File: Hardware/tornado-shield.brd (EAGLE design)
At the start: 439.4 x 100 mm, 30 parts, among them CON1 ROV_SHIELD_V2, Q1 DMP2012SN-7, U1 LM2678S-5.0, U2 LM3409HV'LM3409HV'

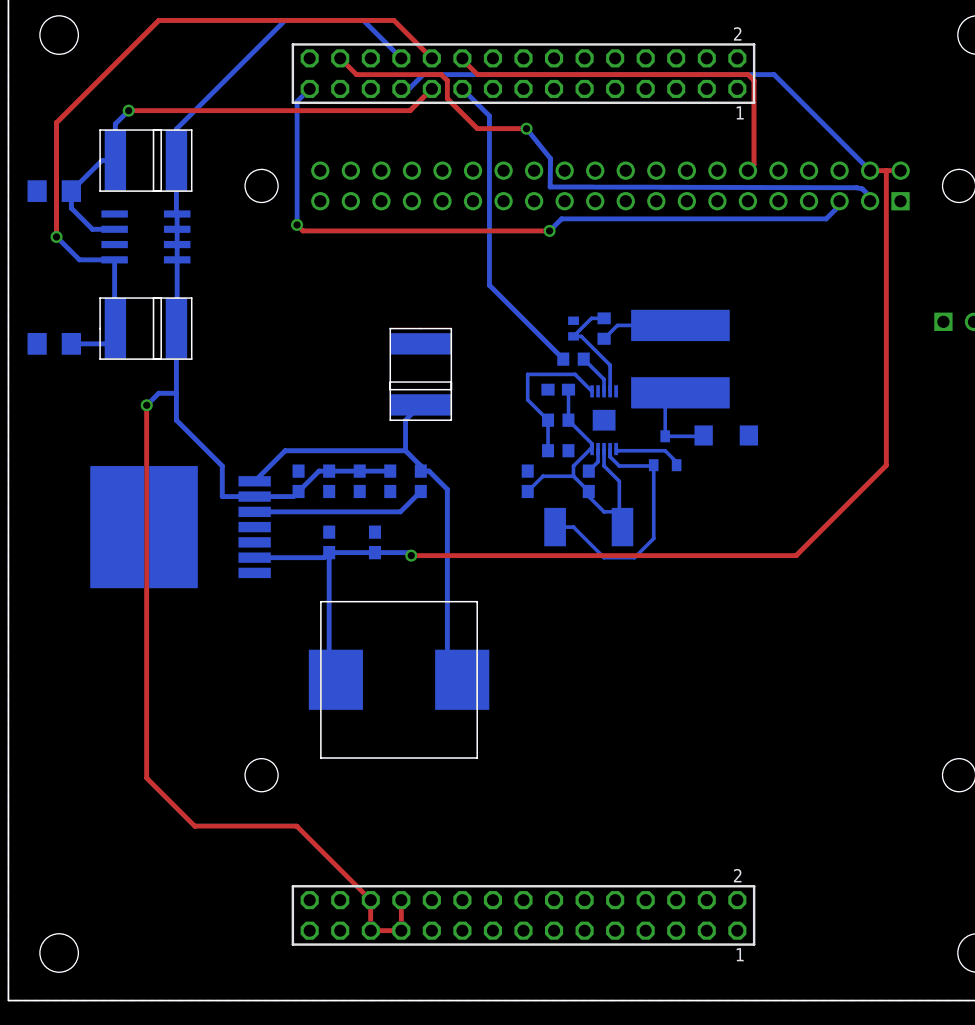
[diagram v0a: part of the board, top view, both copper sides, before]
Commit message: Continued to finish Shield
Still needs Pi Pinout
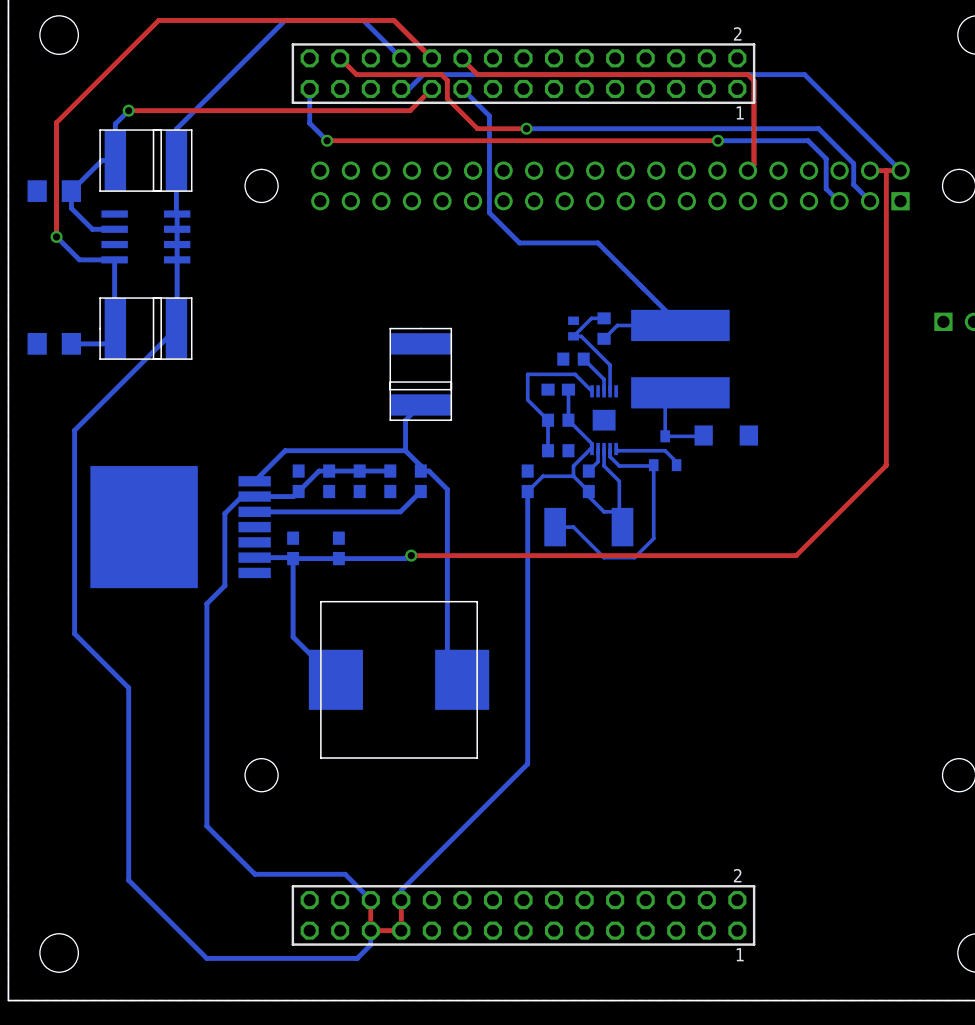
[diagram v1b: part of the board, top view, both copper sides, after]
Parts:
- moved C2 3.04 mm to (23.7, 37.6)
- moved C3 3.04 mm to (27.5, 37.6)
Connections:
- removed net V_IN: C_F.1, C_IN1.1, C_IN2.1, R_SNS.2, R_UV2.2, U2.10, U2.8
- removed net V_OUT: L2.2, R_OFF.1
- new net LED_CON: R_PD.1
- net +12V: now also C_F.1, C_IN1.1, C_IN2.1, R_SNS.2, R_UV2.2, U2.10, U2.8
- net LED_PWM: now also L2.2, R_OFF.1; no longer R_PD.1
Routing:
- net +12V: track 135.1 -> 245.6 mm, vias 1 -> 0
- net V_IN: track 25.5 -> 0.00 mm
- net LED_PWM: track 25.9 -> 37.8 mm
- net NAV_SCL: track 58.3 -> 51.1 mm
- net V_OUT: track 6.81 -> 0.00 mm
- net +5V: track 136.6 -> 141.6 mm
- net NAV_SDA: track 51.6 -> 50.9 mm

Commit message: Wrapping up initial board layout
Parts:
- added RPD, RPD1: 1k, DiscreteComponents:R0603
- moved L1 1.50 mm to (31.0, 26.7)
- moved U$4 0.50 mm to (11.4, 55.4)
- moved U$5 0.50 mm to (11.4, 70.3)
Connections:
- removed net LED_PMW: CON1.18
- removed net N$23: CON1.14
- removed net SCL: CON1.20
- removed net SDA: CON1.22
- new net +3V3: U$2.1
- new net SONAR_TIMER: CON1.14, U$2.36
- net GND: now also RPD.1, RPD1.1
- net GPIO: now also U$2.7
- net GPIO2: now also U$2.11
- net GPIO3: now also U$2.13
- net GPIO4: now also U$2.15
- net GPIO5: now also U$2.31
- net GPIO6: now also U$2.38
- net GPIO7: now also U$2.40
- net LED_CON: now also U$2.33
- net NAV_SCL: now also CON1.20
- net NAV_SDA: now also CON1.22
- net SOL1_IN: now also RPD1.2, U$2.35
- net SOL2_IN: now also RPD.2, U$2.37
- net SONAR_PWM: now also U$2.32
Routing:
- net GPIO: track 0.00 -> 97.5 mm
- net GPIO2: track 0.00 -> 94.8 mm
- net NAV_SDA: track 50.9 -> 145.4 mm, vias 1 -> 2
- net GPIO3: track 0.00 -> 90.2 mm
- net GPIO4: track 0.00 -> 80.7 mm
- net GPIO7: track 0.00 -> 67.3 mm, vias 0 -> 2
- net SONAR_TIMER: track 0.00 -> 66.6 mm, vias 0 -> 2
- net NAV_SCL: track 51.1 -> 117.3 mm
- net GPIO5: track 0.00 -> 63.5 mm, vias 0 -> 3
- net GPIO6: track 0.00 -> 56.3 mm, vias 0 -> 1
- net SOL1_IN: track 0.00 -> 34.0 mm, vias 0 -> 2
- net SOL2_IN: track 0.00 -> 27.0 mm, vias 0 -> 2
- net SONAR_PWM: track 0.00 -> 21.1 mm
- net LED_CON: track 0.00 -> 18.3 mm
- net +12V: track 245.6 -> 249.2 mm, vias 0 -> 1
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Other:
- board size 439.4 x 100 mm -> 84.9 x 84 mm

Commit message: Board Design Rev 1.0
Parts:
- moved R_UV1 0.50 mm to (45.7, 46.2)
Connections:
- removed net KJ: CON1.77
- removed net N$10: CON1.1
- removed net N$11: CON1.78
- removed net N$24: CON1.13
- removed net N$25: CON1.12
- removed net N$26: CON1.11
- removed net N$27: CON1.10
- removed net N$28: CON1.9
- removed net N$29: CON1.8
- removed net N$30: CON1.7
- removed net N$31: CON1.6
- removed net N$32: CON1.5
- removed net N$33: CON1.4
- removed net N$34: CON1.3
- removed net N$37: CON1.76
- removed net N$38: CON1.75
- removed net N$39: CON1.74
- removed net N$40: CON1.73
- removed net N$41: CON1.72
- removed net N$42: CON1.71
- removed net N$43: CON1.70
- removed net N$44: CON1.69
- removed net N$45: CON1.68
- removed net N$46: CON1.67
- removed net N$47: CON1.66
- removed net N$48: CON1.65
- removed net N$49: CON1.64
- removed net N$50: CON1.63
- removed net N$6: U$2.6
- removed net N$9: CON1.2
- net GND: now also U$2.6
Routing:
- net +5V: track 140.9 -> 166.6 mm
- net +12V: track 249.2 -> 246.7 mm
- net NAV_SCL: track 117.3 -> 115.4 mm
- net N$2: track 13.0 -> 12.5 mm
- net SONAR_TIMER: vias 2 -> 1
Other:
- board text added: "Board made by Sam Deghuee and Flor Albornoz, with help from Matt Molo Purdue ROV 2016"

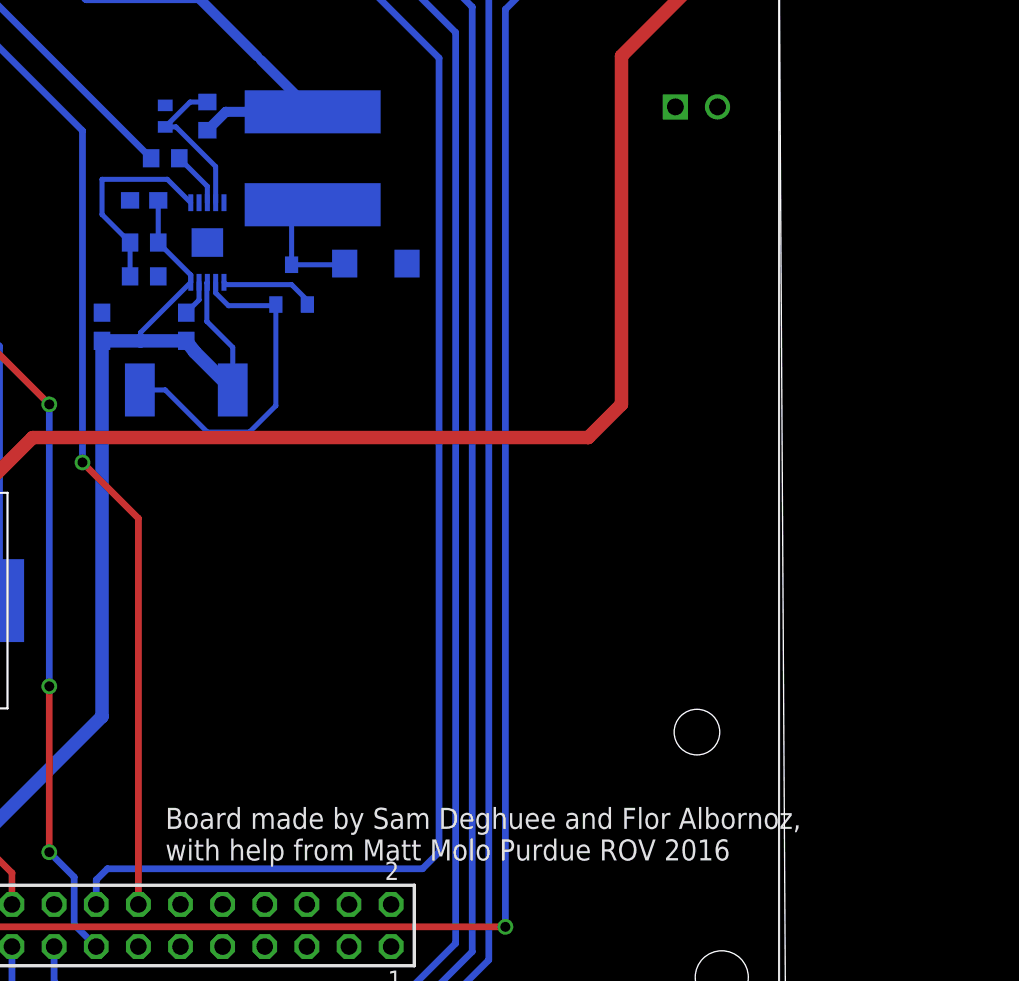
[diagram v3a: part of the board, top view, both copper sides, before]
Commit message: Post Nick recomendations
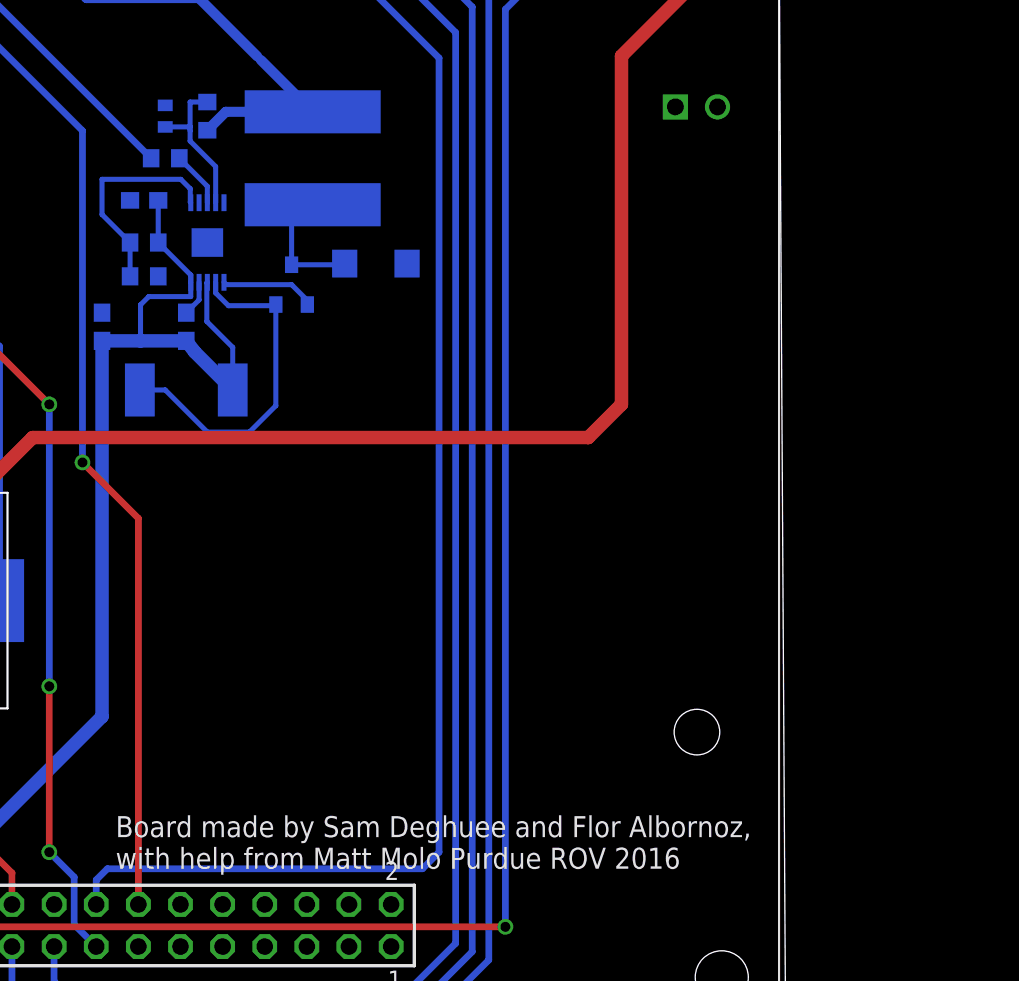
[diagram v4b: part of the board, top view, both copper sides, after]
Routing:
- net +12V: track 246.7 -> 248.1 mm
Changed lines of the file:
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@@
 <rectangle x1="13.79536875" y1="14.465190625" x2="13.97316875" y2="14.482971875" layer="21"/>
 <rectangle x1="13.79536875" y1="14.482971875" x2="13.84870625" y2="14.500746875" layer="21"/>
-<text x="47" y="11" size="1.27" layer="21">Board made by Sam Deghuee and Flor Albornoz,
+<text x="44" y="10.5" size="1.27" layer="21">Board made by Sam Deghuee and Flor Albornoz,
 with help from Matt Molo Purdue ROV 2016</text>
 </plain>
@@
 <wire x1="51.06" y1="41.94" x2="51.06" y2="39.37" width="0.3048" layer="16"/>
 <wire x1="48.529240625" y1="45.8597" x2="48.529240625" y2="46.300759375" width="0.3048" layer="16"/>
-<wire x1="48.529240625" y1="45.8597" x2="45.5" y2="42.830459375" width="0.3048" layer="16"/>
-<wire x1="45.5" y1="42.830459375" x2="45.5" y2="42.33" width="0.3048" layer="16"/>
+<wire x1="45.5" y1="42.33" x2="45.5" y2="44.5" width="0.3048" layer="16"/>
+<wire x1="45.5" y1="44.5" x2="46" y2="45" width="0.3048" layer="16"/>
+<wire x1="46" y1="45" x2="48.529240625" y2="45" width="0.3048" layer="16"/>
+<wire x1="48.529240625" y1="45" x2="48.529240625" y2="45.8597" width="0.3048" layer="16"/>
 </signal>
 <signal name="N$3">
@@
 <contactref element="U2" pad="1"/>
 <wire x1="44.87" y1="46.22" x2="44.87" y2="48.26" width="0.3048" layer="16"/>
-<wire x1="48.529240625" y1="50.6603" x2="47.119540625" y2="52.07" width="0.3048" layer="16"/>
-<wire x1="47.119540625" y1="52.07" x2="43.18" y2="52.07" width="0.3048" layer="16"/>
+<wire x1="47.93" y1="52.07" x2="43.18" y2="52.07" width="0.3048" layer="16"/>
 <wire x1="43.18" y1="52.07" x2="43.18" y2="49.95" width="0.3048" layer="16"/>
 <wire x1="43.18" y1="49.95" x2="44.87" y2="48.26" width="0.3048" layer="16"/>
+<wire x1="47.93" y1="52.07" x2="48.5" y2="51.5" width="0.3048" layer="16"/>
+<wire x1="48.5" y1="51.5" x2="48.5" y2="50.689540625" width="0.3048" layer="16"/>
+<wire x1="48.5" y1="50.689540625" x2="48.529240625" y2="50.6603" width="0.3048" layer="16"/>
 </signal>
 <signal name="N$1">
@@
 <contactref element="U2" pad="4"/>
 <wire x1="49.53" y1="56.73" x2="48.49" y2="56.73" width="0.3048" layer="16"/>
-<wire x1="48.49" y1="56.73" x2="46.99" y2="55.23" width="0.3048" layer="16"/>
-<wire x1="46.99" y1="55.23" x2="47.64" y2="55.23" width="0.3048" layer="16"/>
-<wire x1="47.64" y1="55.23" x2="50.03038125" y2="52.83961875" width="0.3048" layer="16"/>
 <wire x1="50.03038125" y1="52.83961875" x2="50.03038125" y2="50.6603" width="0.3048" layer="16"/>
+<wire x1="48.49" y1="56.73" x2="48.49" y2="55.23" width="0.3048" layer="16"/>
+<wire x1="48.49" y1="55" x2="48.49" y2="54.38" width="0.3048" layer="16"/>
+<wire x1="48.49" y1="54.38" x2="50.03038125" y2="52.83961875" width="0.3048" layer="16"/>
+<wire x1="46.99" y1="55.23" x2="48.49" y2="55.23" width="0.3048" layer="16"/>
+<wire x1="48.49" y1="55.23" x2="48.49" y2="55" width="0.3048" layer="16"/>
 </signal>
 <signal name="N$8">

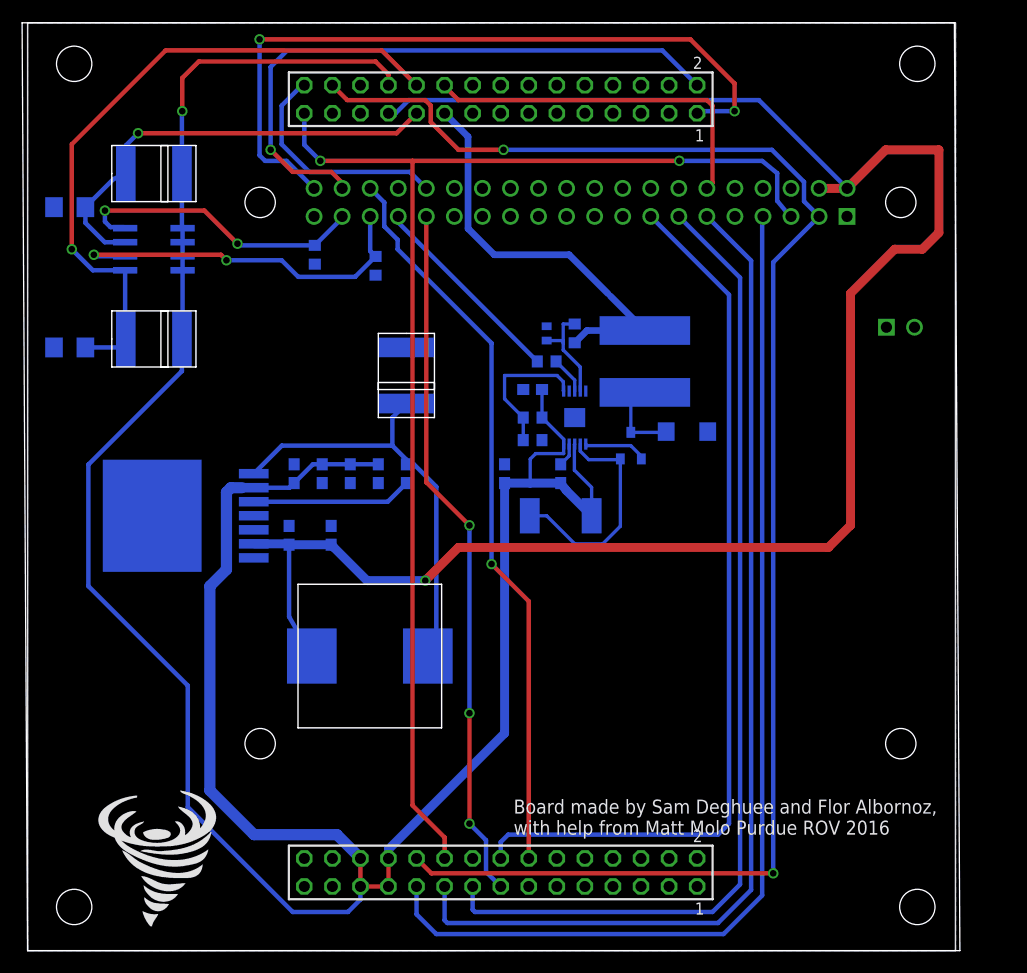
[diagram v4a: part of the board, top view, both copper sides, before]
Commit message: Fixes from Michael
Mostly layout, fixing ground islands, and other small fixes.
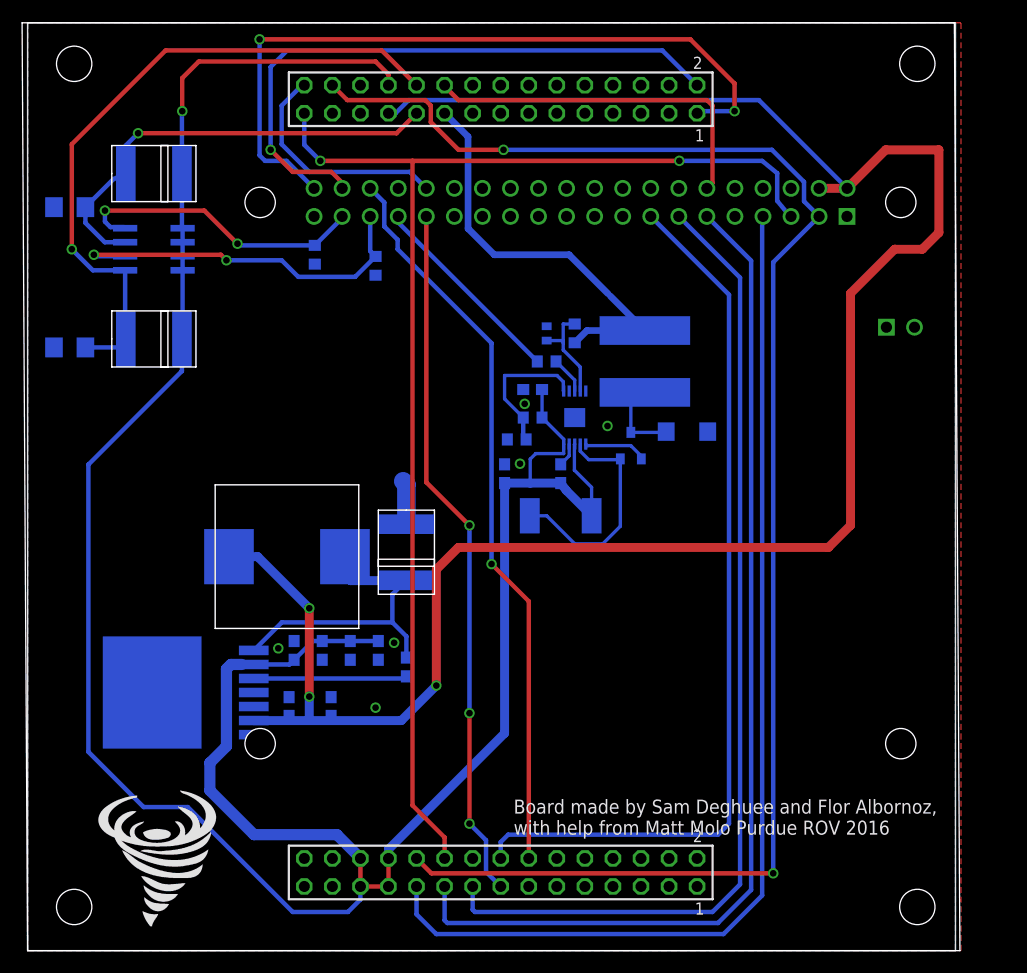
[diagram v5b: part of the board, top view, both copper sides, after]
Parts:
- moved C1 17.5 mm to (34.3, 25.7)
- moved C4 16.0 mm to (24.1, 27.2)
- moved C5 16.0 mm to (26.7, 27.2)
- moved C6 16.0 mm to (29.2, 27.2)
- moved C7 16.0 mm to (31.8, 27.2)
- moved U$3 16.0 mm to (34.3, 36.1)
- moved U1 16.0 mm to (11.4, 23.4)
- moved C2 15.5 mm to (23.7, 22.1)
- moved C3 15.5 mm to (27.5, 22.1)
- moved L1 11.7 mm to (23.5, 35.7)
- moved R_UV1 1.44 mm to (44.3, 46.3), turned to 180 degrees
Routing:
- net +5V: track 166.6 -> 184.2 mm, vias 1 -> 3
- net +12V: track 248.1 -> 234.5 mm
- net SWOUT: track 39.7 -> 29.0 mm
- net GND: track 0.00 -> 4.80 mm, vias 0 -> 6
- net N$3: track 14.5 -> 14.0 mm
- added copper zone on layer 1, net GND
